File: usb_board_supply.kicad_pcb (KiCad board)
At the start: 2 copper layers, 37.3 x 11.9 mm, 9 parts, among them J1 USB_B_Micro, J2 Conn_01x02, J3 Conn_01x02, SW1 SW_DPST

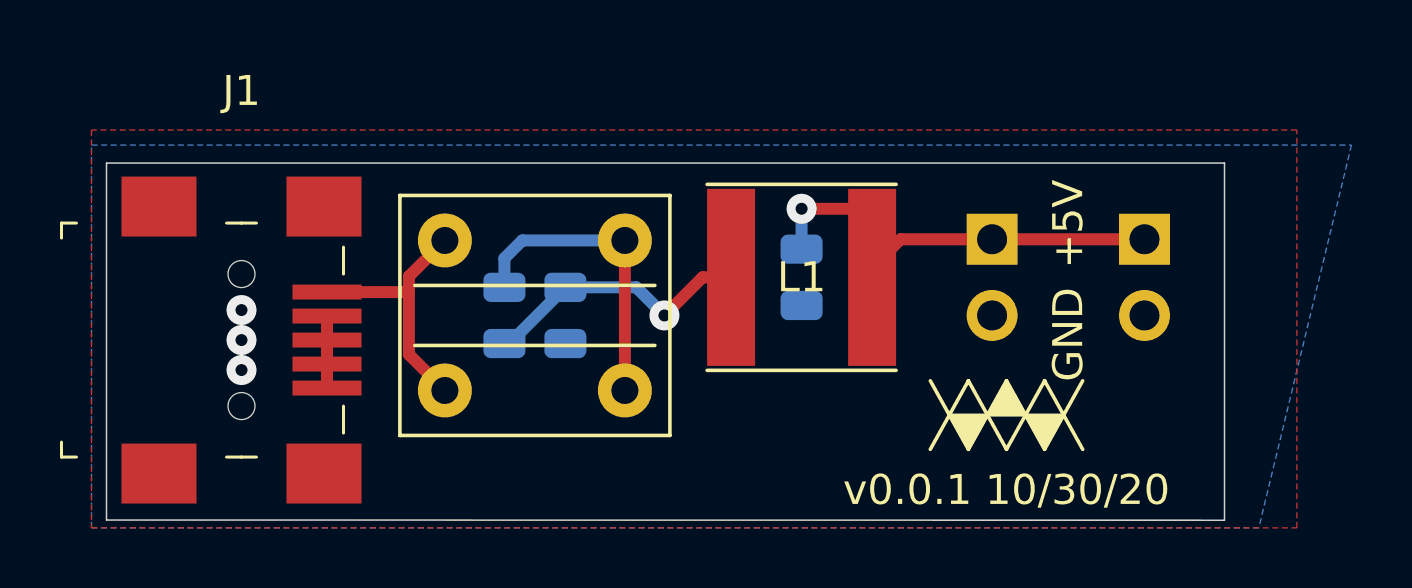
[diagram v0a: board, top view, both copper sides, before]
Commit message: Update to use mosfet instead of switch
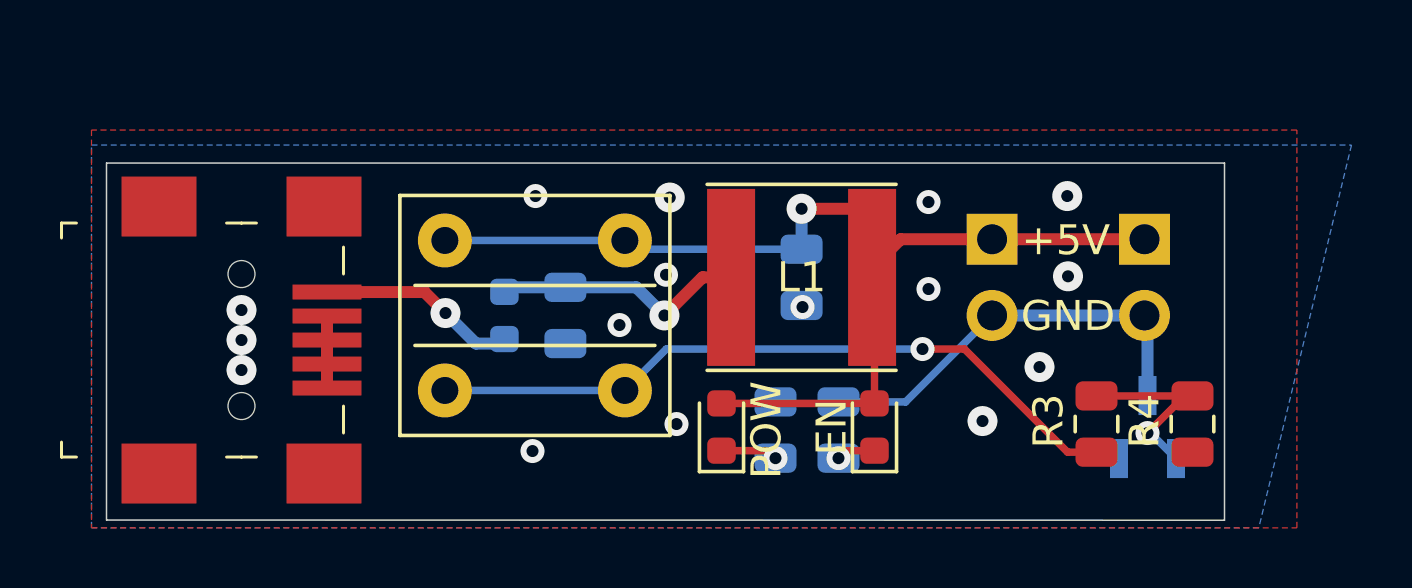
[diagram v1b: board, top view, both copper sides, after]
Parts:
- added EN: EN, LED_SMD:LED_0603_1608Metric, F.Cu at (156.1, 110.4)
- added POW: POW, LED_SMD:LED_0603_1608Metric, F.Cu at (151.0, 110.4)
- added R1: 10kR, Resistor_SMD:R_0805_2012Metric, B.Cu at (154.9, 110.5)
- added R2: 10kR, Resistor_SMD:R_0805_2012Metric, B.Cu at (152.8, 110.5)
- added R3: 10kR, Resistor_SMD:R_0805_2012Metric, F.Cu at (163.5, 110.3)
- added R4: 1MR, Resistor_SMD:R_0805_2012Metric, F.Cu at (166.7, 110.3)
- added e1: BSS138, digikey-footprints:SOT-23-3, B.Cu at (165.2, 110.4)
- F1: value 1A -> 2A; footprint Fuse:Fuse_0805_2012Metric -> Fuse:Fuse_0603_1608Metric
- REF**: moved to B.Cu
- SW1: value SW_DPST -> ON/OFF
- moved REF** 28.3 mm to (132.3, 107.6), turned to 270 degrees
- turned F1 to 270 degrees
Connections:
- F1 pad 2: Net-(F1-Pad2) -> V+
- J2 pad 2: GND -> V0UT
- J3 pad 2: GND -> V0UT
- SW1 pad 1: V+ -> VFILT
- SW1 pad 2: Net-(F1-Pad2) -> Net-(R3-Pad1)
- SW1 pad 3: V+ -> VFILT
- SW1 pad 4: Net-(F1-Pad2) -> Net-(R3-Pad1)
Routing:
- net Net-(R3-Pad1): track 0.00 -> 23.7 mm, vias 0 -> 1
- net VFILT: track 15.4 -> 36.7 mm
- net V0UT: track 0.00 -> 14.1 mm
- net Net-(F1-Pad2): track 10.2 -> 0.00 mm
- net Net-(R3-Pad2): track 0.00 -> 6.51 mm, vias 0 -> 1
- net V+: track 8.73 -> 6.78 mm, vias 0 -> 1
- net Net-(D2-Pad1): track 0.00 -> 1.90 mm, vias 0 -> 1
- net Net-(D1-Pad1): track 0.00 -> 1.30 mm, vias 0 -> 1
- net Net-(C1-Pad1): track 9.25 -> 8.47 mm
- net GND: vias 3 -> 16
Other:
- board text added: "v0.0.2 11/09/20"
- board text removed: "v0.0.1 10/30/20"
